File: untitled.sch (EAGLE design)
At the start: 26 parts, among them J3 CORTEX_DEBUG_PTH, J6 USB-MICROB, U1 ATSAMD21G-M, U2 MIC5501-3.0YM5-TR, U3 TPD2S017, Y1 32.768KHZ

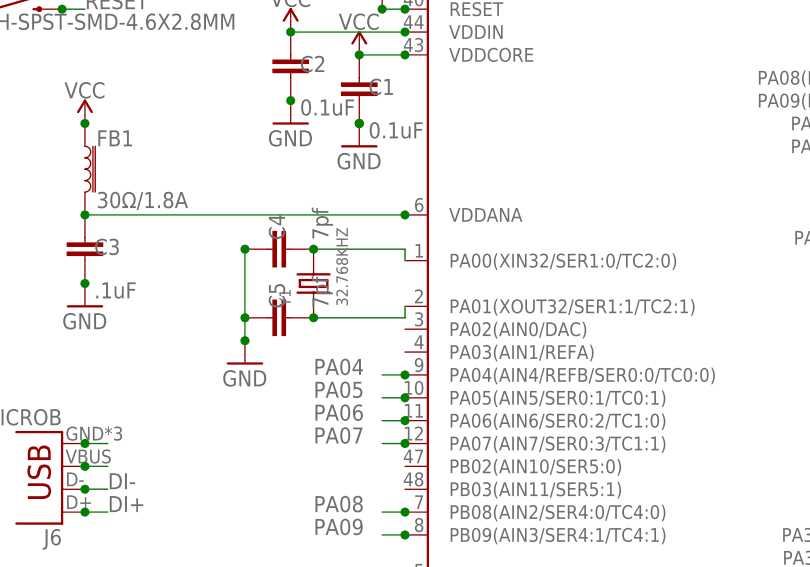
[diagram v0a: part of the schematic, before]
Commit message: added via to button pullup
added a via to the button pullup to shorten distance to ground.
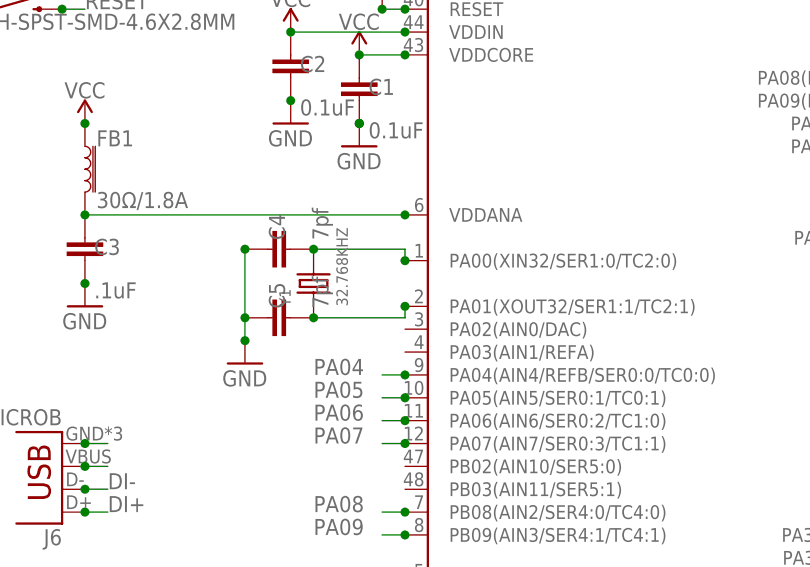
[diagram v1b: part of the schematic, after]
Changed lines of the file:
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@@
 <pinref part="C5" gate="G$1" pin="2"/>
 <junction x="149.86" y="113.03"/>
+<junction x="160.02" y="114.3"/>
 </segment>
 </net>
@@
 <pinref part="C4" gate="G$1" pin="2"/>
 <junction x="149.86" y="120.65"/>
+<junction x="160.02" y="119.38"/>
 </segment>
 </net>
